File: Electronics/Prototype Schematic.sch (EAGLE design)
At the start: 17 parts, among them IC1 A3144, IC2 A3144, IC3 A3144, IC4 A3144

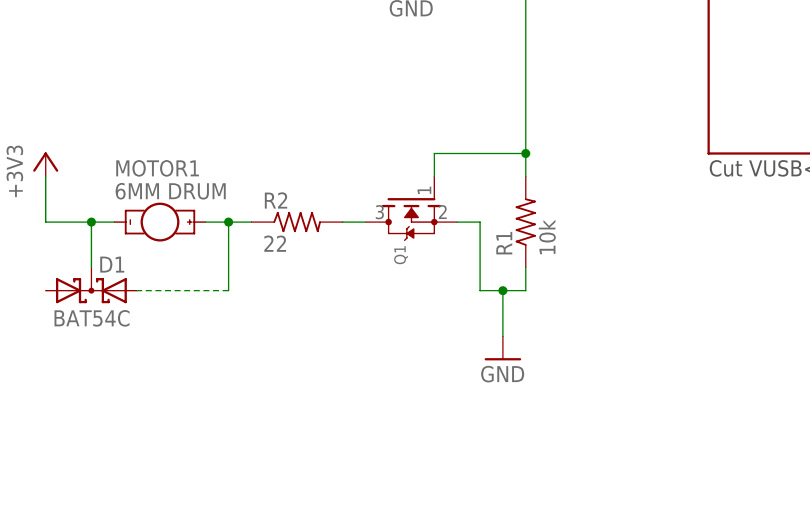
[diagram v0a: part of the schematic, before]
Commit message: Added PDF Schematic
Also added part name for Q1
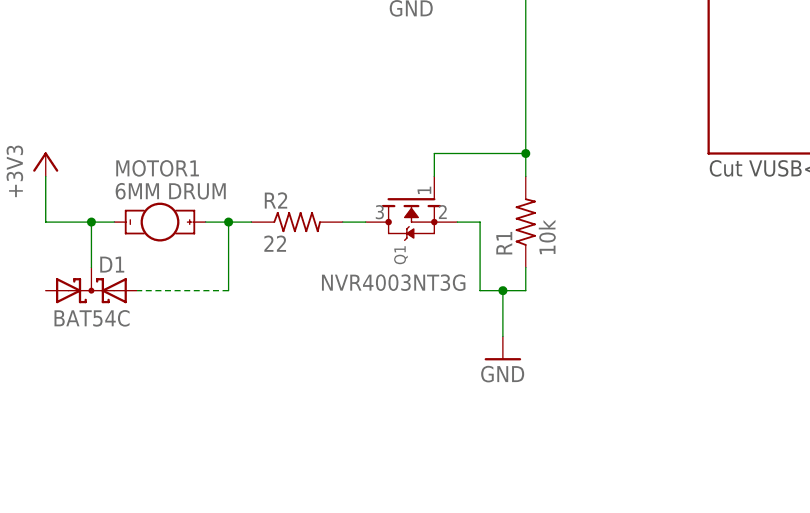
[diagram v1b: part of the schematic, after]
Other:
- note added: "NVR4003NT3G"
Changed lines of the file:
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@@
 pointer and thumb</text>
 <text x="-12.7" y="132.08" size="1.778" layer="97">Place on knuckles</text>
+<text x="-58.42" y="-53.34" size="1.778" layer="95">NVR4003NT3G</text>
 </plain>
 <instances>
